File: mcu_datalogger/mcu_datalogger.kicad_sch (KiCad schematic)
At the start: 25 parts, among them U1 24LC1025, U2 24LC1025, U3 DS1337S_, U4 ATMEGA328P-AU, Y1 32.768 KHz, Y2 16 MHz

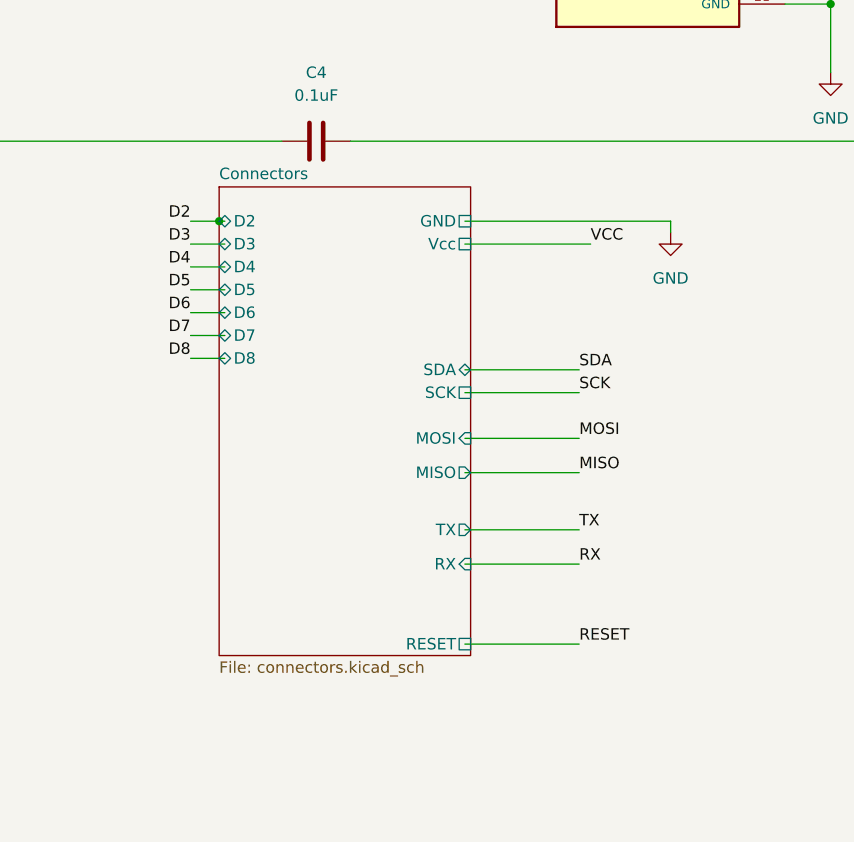
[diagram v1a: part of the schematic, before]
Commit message: fix stupid hierarchical label issue
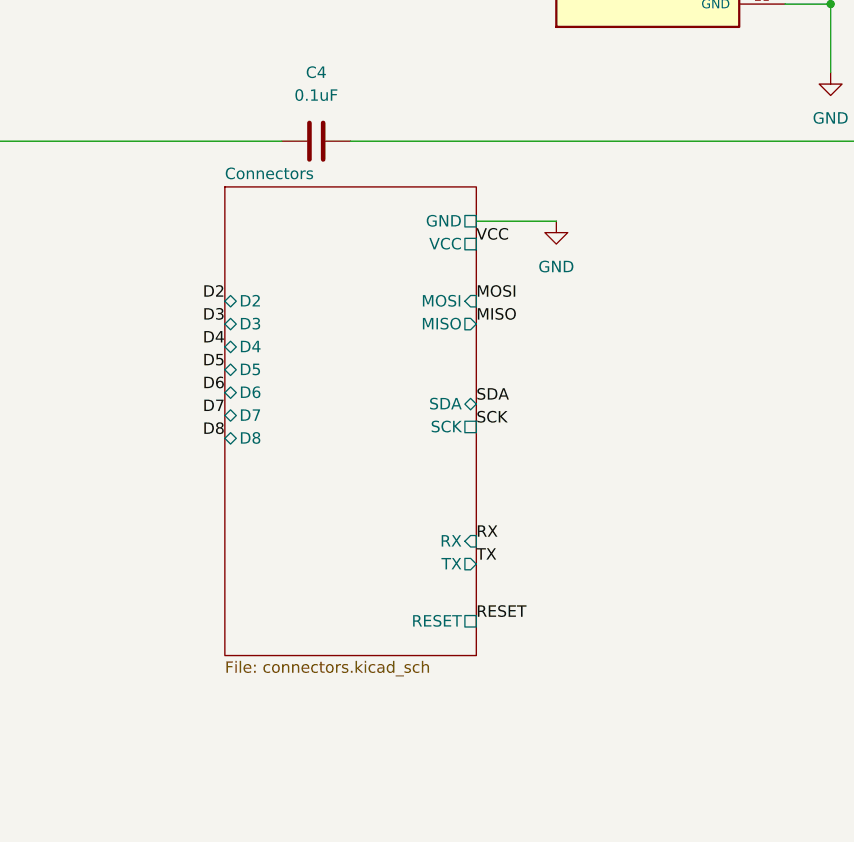
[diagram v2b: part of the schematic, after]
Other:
- sheet Connectors ports: added VCC; removed Vcc

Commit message: add comments
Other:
- note added: "EEPROM"
- note added: "MCU"
- note added: "Mounting"
- note added: "Real Time Clock"
- moved on the sheet: BT1, C2, C3, C4, C5, D1, D2, H1, H2, H3, H4, R1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
